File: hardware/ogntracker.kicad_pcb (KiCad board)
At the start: 2 copper layers, 82.7 x 56.6 mm, 79 parts, among them J1 ANT, J2 SWD, J3 BOOT, J4 IGC, J5 Micro USB, SW1 RESET, U1 LM2936-3.3, Y1 32.768K, Y2 8MHz, Y3 12M

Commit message: v0.6 routed
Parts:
- removed C13: 22pF, Capacitors_SMD:C_0603_HandSoldering
- removed C24: 100nF, Capacitors_SMD:C_0805
- removed CPU1: STM32F103, Housings_QFP:LQFP-48_7x7mm_Pitch0.5mm
- removed D2: STATUS_PANEL, OGN Tracker:Molex_PicoBlade_02x1.25mm_HandSoldering
- removed D3: STATUS_SMD, LEDs:LED_0603
- removed D4: PWR, LEDs:LED_0603
- removed D5: LED_BT, OGN Tracker:Molex_PicoBlade_02x1.25mm_HandSoldering
- removed R19: 1.5K, Resistors_SMD:R_0805
- removed Y1: 32.768K, Crystals:Crystal_SMD_SeikoEpson_MC306-4pin_8.0x3.2mm
- added J6: BT_KEY, Pin_Headers:Pin_Header_Straight_2x01_Pitch2.54mm, F.Cu at (113.2, 94.7)
- added J7: UART, Pin_Headers:Pin_Header_Straight_1x04_Pitch2.54mm, F.Cu at (148.3, 55.0)
- added LED1: STATUS_PANEL, LEDs:LED_D5.0mm_Horizontal_O3.81mm_Z3.0mm, F.Cu at (107.6, 47.9)
- added LED2: STATUS_SMD, LEDs:LED_0603, F.Cu at (132.6, 90.7)
- added LED3: LED_BT, LEDs:LED_D5.0mm_Horizontal_O3.81mm_Z3.0mm, F.Cu at (107.6, 55.5)
- added LED4: LED_BT_STATUS, LEDs:LED_0603, F.Cu at (114.7, 76.9)
- added LED5: PWR, LEDs:LED_0603, F.Cu at (113.0, 47.4)
- added MCU1: STM32F103, Housings_QFP:LQFP-48_7x7mm_Pitch0.5mm, F.Cu at (139.0, 64.8)
- BARO1: footprint OGN Tracker:BMP280_HandSoldering -> KDR Tracker:BMP280
- BT1: value JDY-08 -> HC-05; footprint OGN Tracker:JDY-08 -> KDR Tracker:HC-05
- C12: value 22pF -> 1uF; footprint Capacitors_SMD:C_0603_HandSoldering -> Capacitors_SMD:C_1206
- C14, C15, C25, C26: footprint Capacitors_SMD:C_0603_HandSoldering -> Capacitors_SMD:C_0603
- C16, C18, C2, D1, D7, D8, F1, R1, R10, R12, R13, R15, R16, R7, R9, Y3: moved to F.Cu
- C27: footprint Capacitors_SMD:C_0805 -> Capacitors_SMD:C_1206
- GPS1: footprint Pin_Headers:Pin_Header_Straight_1x06_Pitch2.00mm -> KDR Tracker:Molex_PicoBlade_53047-0610_06x1.25mm_Straight
- J1: footprint OGN Tracker:IPEX -> KDR Tracker:SMA_CONN
- J3: footprint Pin_Headers:Pin_Header_Straight_2x03_Pitch2.54mm -> Pin_Headers:Pin_Header_Straight_2x01_Pitch2.54mm
- J4: footprint OGN Tracker:RJ45_SOCKET_SHLD -> KDR Tracker:RJ45_SOCKET_SHLD
- J5: footprint OGN Tracker:USB_Micro -> KDR Tracker:USB_Micro
- PWR1: footprint OGN Tracker:Buck_Converter_Sm_HandSoldering -> KDR Tracker:Buck_Converter_Sm
- R17: value 20 -> 100K; moved to F.Cu
- R18: value 20 -> 520; moved to F.Cu
- RF1: footprint OGN Tracker:RFM69HW -> KDR Tracker:RFM69HW
- SDCARD1: footprint OGN Tracker:SDCARD_BOMB -> KDR Tracker:SDCARD_BOMB
- Y2: footprint Crystals:Crystal_HC49-4H_Vertical -> Crystals:Crystal_SMD_HC49-SD; moved to F.Cu
- moved R17 78.9 mm to (110.2, 95.2), turned to 270 degrees
- moved R18 64.4 mm to (114.7, 75.4)
- moved J3 52.9 mm to (118.8, 51.8), turned to 0 degrees
- moved C16 49.4 mm to (128.4, 47.4), turned to 0 degrees
- moved BARO1 46.7 mm to (129.5, 47.6), turned to 180 degrees
- moved J1 44.4 mm to (178.2, 92.9), turned to 270 degrees
- moved R10 43.9 mm to (128.4, 49.2), turned to 180 degrees
- moved R13 43.4 mm to (124.6, 51.2), turned to 0 degrees
- moved R3 43.0 mm to (113.0, 49.2)
- moved C5 41.8 mm to (133.3, 96.7)
- moved R1 41.6 mm to (105.1, 49.2), turned to 90 degrees
- moved R12 40.4 mm to (124.6, 53.3), turned to 0 degrees
- moved C19 40.2 mm to (149.8, 64.4), turned to 270 degrees
- moved C21 39.5 mm to (149.8, 68.2), turned to 270 degrees
- moved C23 39.4 mm to (149.8, 72.0), turned to 90 degrees
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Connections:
- BT1 pad 1: 3.3V -> Net-(BT1-Pad1)
- BT1 pad 12: (no net) -> 3.3V
- BT1 pad 13: (no net) -> Earth
- BT1 pad 19: /Console/BT_TX -> (no net)
- BT1 pad 2: (no net) -> /CON1_TXD
- BT1 pad 20: /CON1_TXD -> (no net)
- BT1 pad 21: (no net) -> Earth
- BT1 pad 24: Earth -> (no net)
- BT1 pad 6: /Console/BT_STATUS -> (no net)
- C12 pad 1: /RTCOUT -> 3.3V
- C14 pad 2: Earth -> Earth_Protective
- C15 pad 2: Earth -> Earth_Protective
- C8 pad 1: Earth -> 3.3V
- C8 pad 2: 3.3V -> Earth
- D7 pad 1: /Console/BT_TX -> Net-(BT1-Pad1)
- F2 pad 1: /5V_PROT -> 5V
- F2 pad 2: 5V -> /5V_PROT
- J3 pad 2: 3.3V -> Net-(J3-Pad2)
- R12 pad 1: Net-(J3-Pad3) -> Net-(J3-Pad2)
- R13 pad 1: /BOOT1 -> Net-(J3-Pad2)
- R13 pad 2: Net-(J3-Pad4) -> Earth
- R15 pad 1: /Console/BT_TX -> Net-(BT1-Pad1)
- R17 pad 1: /USB_D+ -> Earth
- R17 pad 2: /Console/CON_USB_D+ -> /Console/BT_KEY
- R18 pad 1: /USB_D- -> 3.3V
- R18 pad 2: /Console/CON_USB_D- -> Net-(LED4-Pad2)
- R7 pad 1: /Console/BT_STATUS -> /Console/BT_PAIRED
- RF1 pad 2: /AUX_STATUS -> /RF_AUXSTAT
- RF1 pad 7: /INT_REQ -> /RF_IRQ
- RF1 pad 8: /CHIP_RESET -> /RF_RESET
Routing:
- net /USB_D+: track 62.1 -> 0.00 mm, vias 3 -> 0
- net /USB_D-: track 59.3 -> 0.00 mm, vias 3 -> 0
- net /BOOT1: track 47.1 -> 0.00 mm, vias 3 -> 0
- net /STAT_LED: track 25.5 -> 72.5 mm, vias 1 -> 3
- net /BUZ_IN: track 64.6 -> 19.9 mm, vias 3 -> 2
- net /CHIP_RESET: track 44.5 -> 0.00 mm, vias 2 -> 0
- net /CON1_RXD: track 153.7 -> 110.1 mm, vias 3 -> 2
- net /CON1_TXD: track 169.3 -> 126.1 mm, vias 6 -> 3
- net Earth_Protective: track 0.00 -> 43.1 mm, vias 0 -> 12
- net /BUZ_OUT: track 54.8 -> 13.6 mm, vias 3 -> 1
- net /INT_REQ: track 39.5 -> 0.00 mm, vias 2 -> 0
- net /RF_AUXSTAT: track 0.00 -> 36.4 mm
- net /Console/CON_USB_D-: track 8.24 -> 41.2 mm, vias 1 -> 0
- net /Console/BT_PAIRED: track 0.00 -> 30.4 mm, vias 0 -> 2
- net 3.3V: track 377.6 -> 347.3 mm, vias 18 -> 22
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- added copper zone on B.Cu, net Earth_Protective
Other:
- net class ANT: via_dia 1.2 -> 0.6; via_drill 0.6 -> 0.4
- net class Default: clearance 0.24 -> 0.2; trace_width 0.24 -> 0.2; via_dia 1.2 -> 0.6; via_drill 0.6 -> 0.4
- net class HV: via_dia 1.8 -> 0.6; via_drill 0.6 -> 0.4
- net class PWR: via_dia 1.6 -> 0.6; via_drill 0.6 -> 0.4
- rule pad_to_mask_clearance: 0.2 -> 0.05
- rule trace_clearance: 0.24 -> 0.2
- board text removed: "Ked Tracker v0.5 by Andrey Lebedev on November 2017"
- board text removed: "Ked Tracker v0.5 for Hammond 1593L"

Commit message: Labels and slight tweaks for 0.6
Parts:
- added REF***: KiCad-Logo2_8mm_SilkScreen, Symbols:KiCad-Logo2_8mm_SilkScreen, B.Cu at (106.0, 89.5)
- added REF***: OSHW-Logo_11.4x12mm_SilkScreen, Symbols:OSHW-Logo_11.4x12mm_SilkScreen, B.Cu at (108.0, 69.2)
- moved R13 11.7 mm to (124.6, 62.9), turned to 270 degrees
- moved R12 9.86 mm to (126.7, 62.9), turned to 270 degrees
- moved R2 7.87 mm to (130.8, 82.8), turned to 0 degrees
- moved LED2 7.38 mm to (133.1, 83.3), turned to 270 degrees
- moved R9 6.75 mm to (122.1, 53.5)
- moved R10 6.75 mm to (122.1, 51.5)
- moved J2 5.68 mm to (119.6, 57.1)
- moved J3 5.35 mm to (113.5, 52.2), turned to 90 degrees
- moved R11 4.68 mm to (139.1, 97.5)
- moved R1 4.37 mm to (107.6, 45.6), turned to 0 degrees
- moved R7 4.37 mm to (107.6, 53.3), turned to 0 degrees
- moved C18 2.90 mm to (122.6, 62.9), turned to 270 degrees
- moved LS1 2.36 mm to (124.2, 71.1)
- moved R3 2.09 mm to (113.5, 47.2)
- moved LED5 2.09 mm to (113.5, 45.4)
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- renumbered Y3 to Y1
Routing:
- net /CON1_TXD: track 126.1 -> 106.1 mm
- net Net-(J3-Pad2): track 4.63 -> 19.6 mm
- net /BOOT0: track 23.2 -> 9.01 mm
- net Earth: track 181.1 -> 167.1 mm, vias 37 -> 50
- net 3.3V: track 347.3 -> 356.0 mm
- net /RESET: track 42.6 -> 51.1 mm
- net /BARO_SDA: track 28.1 -> 35.9 mm
- net /CON1_RXD: track 110.1 -> 102.5 mm
- net /SD_MISO: track 46.1 -> 39.7 mm
- net /SD_MOSI: track 43.4 -> 38.0 mm
- net /SD_CS: track 43.2 -> 38.6 mm
- net /SD_SCK: track 44.3 -> 40.3 mm
- net /BARO_SCL: track 30.6 -> 34.2 mm
- net /SWDCLK: track 9.98 -> 13.3 mm, vias 1 -> 2
- net /GPS_PPS: track 34.8 -> 31.7 mm
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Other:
- board text added: "3V3"
- board text added: "B"
- board text added: "CLK"
- board text added: "DIO"
- board text added: "G"
- board text added: "GND"
- board text added: "IGC"
- board text added: "K"
- board text added: "KDR Tracker v0.6"
- board text added: "KDR Tracker v0.6 2017"
- board text added: "Open Glider Network Tracker For Hammond-1593L enclosure Based on design by http://glidernet.org For more info please visit https://github.com/kedder/kedtracker"
- board text added: "R"
- board text added: "RX"
- board text added: "TX"
- board text added: "W"
- board text added: "Y"

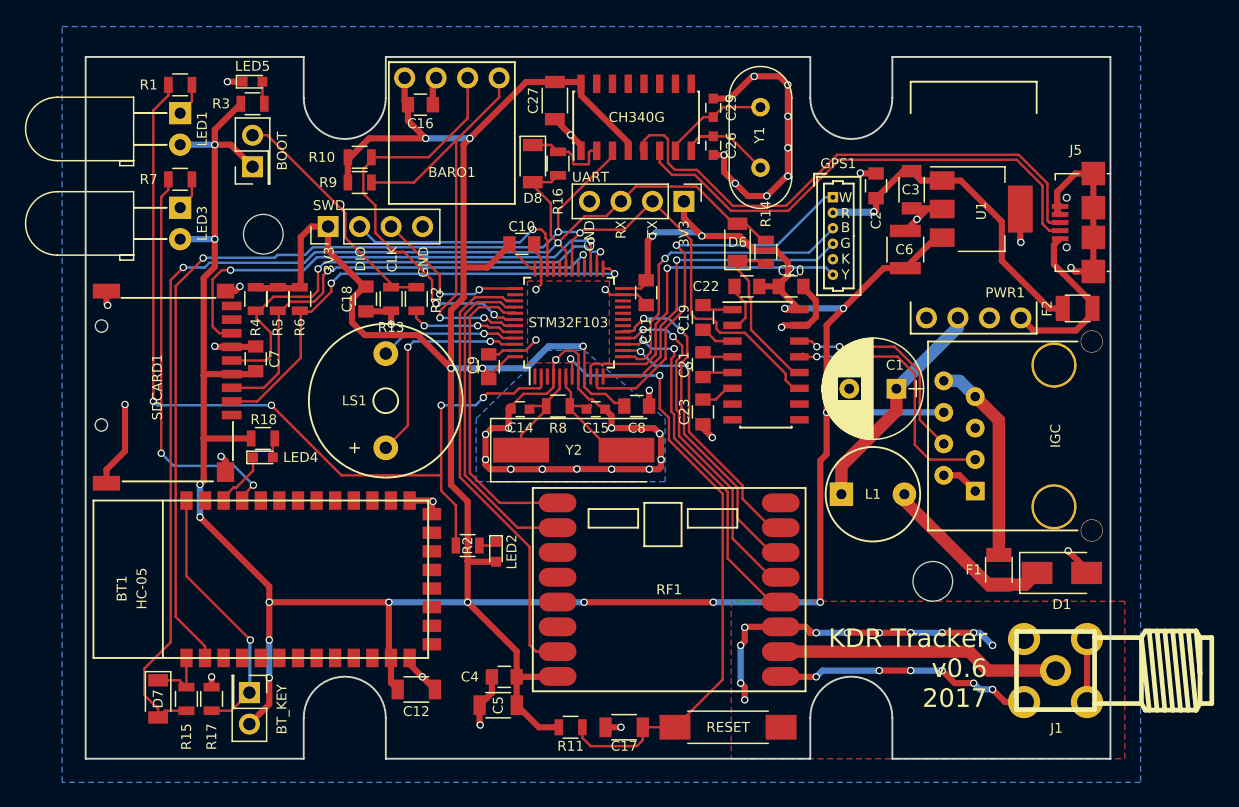
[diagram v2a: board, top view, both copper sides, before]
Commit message: Components renamed to be more uniform
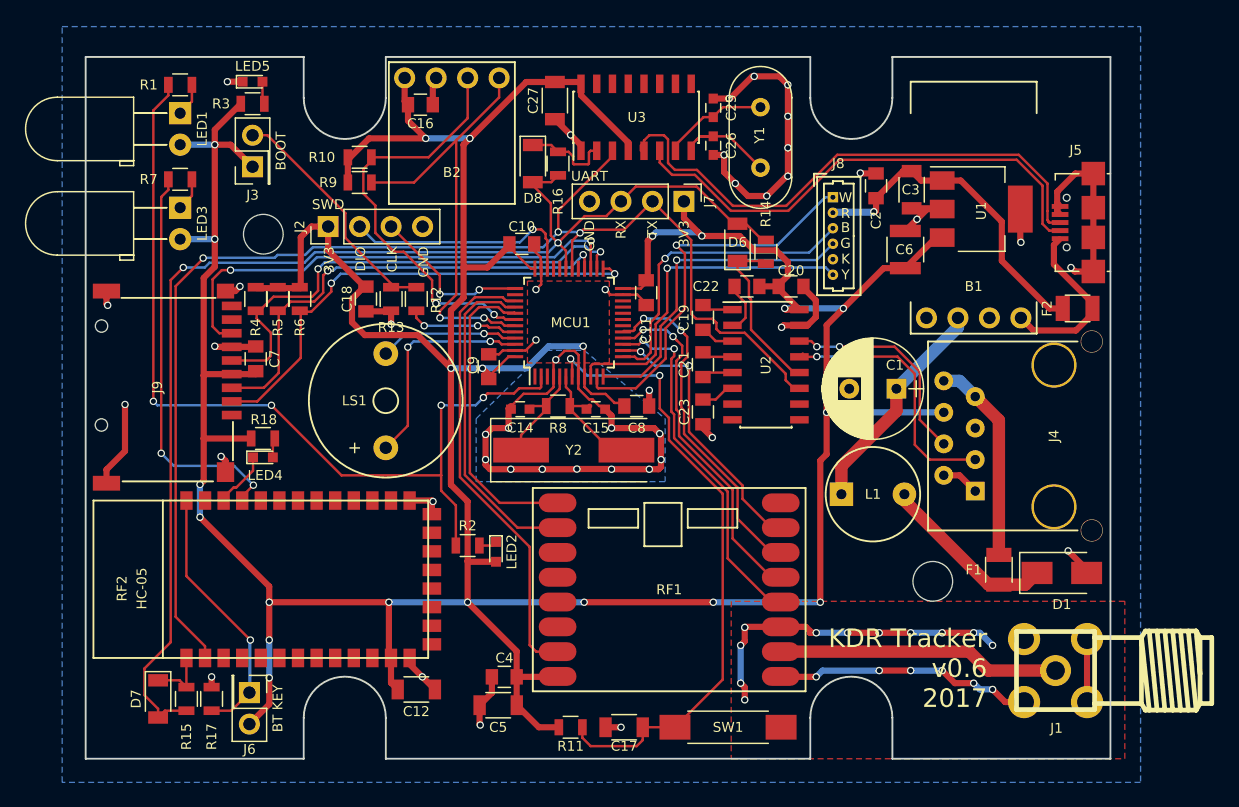
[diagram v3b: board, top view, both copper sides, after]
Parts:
- renumbered PWR1 to B1, BARO1 to B2, GPS1 to J8, SDCARD1 to J9, BT1 to RF2, MAX1 to U2, CH340G1 to U3
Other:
- board text added: "BOOT"
- board text added: "BT KEY"
- board text added: "Open Glider Network Tracker For Hammond-1593L enclosure Based on design by http://glidernet.org For more info please visit https://github.com/kedder/kdrtracker"
- board text added: "SWD"
- board text added: "UART"
- board text removed: "Open Glider Network Tracker For Hammond-1593L enclosure Based on design by http://glidernet.org For more info please visit https://github.com/kedder/kedtracker"

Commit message: More tweaks for new box
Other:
- board text added: "Open Glider Network Tracker For Hammond-1593L enclosure Based on design by http://glidernet.org For more info visit https://github.com/kedder/kdrtracker"
- board text removed: "Open Glider Network Tracker For Hammond-1593L enclosure Based on design by http://glidernet.org For more info please visit https://github.com/kedder/kdrtracker"
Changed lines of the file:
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@@
     (effects (font (size 1.5 1.5) (thickness 0.3)) (justify right))
   )
-  (gr_text "Open Glider Network Tracker\n\nFor Hammond-1593L enclosure\n\nBased on design by http://glidernet.org\nFor more info please visit\nhttps://github.com/kedder/kdrtracker" (at 133.096 98.044 270) (layer B.SilkS)
+  (gr_text "Open Glider Network Tracker\n\nFor Hammond-1593L enclosure\n\nBased on design by http://glidernet.org\nFor more info visit\nhttps://github.com/kedder/kdrtracker" (at 133.096 98.044 270) (layer B.SilkS)
     (effects (font (size 1 1) (thickness 0.15)) (justify left mirror))
   )
